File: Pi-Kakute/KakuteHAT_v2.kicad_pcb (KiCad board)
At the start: 2 copper layers, 65 x 56 mm, 49 parts, among them J1 40HAT, J12 FC_Socket, J2 ID_EEPROM, J3 I2C, J4 Mout1_2, J5 Mout3_4, J6 RC_IN, J7 GPS2, J8 Power_Pad, J9 FC_Socket2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

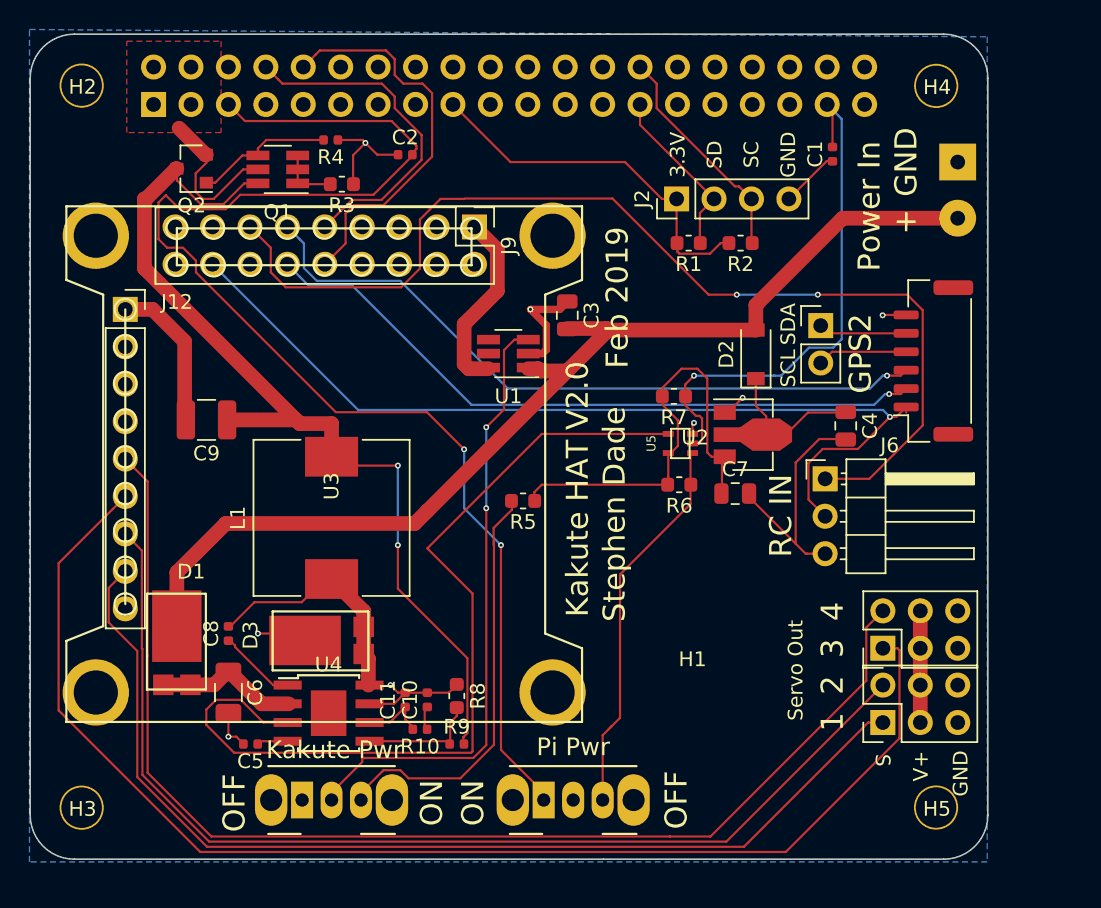
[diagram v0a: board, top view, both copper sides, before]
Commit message: Pi-Kakute: Added EEPROM and improved 40-pin header and mounting holes
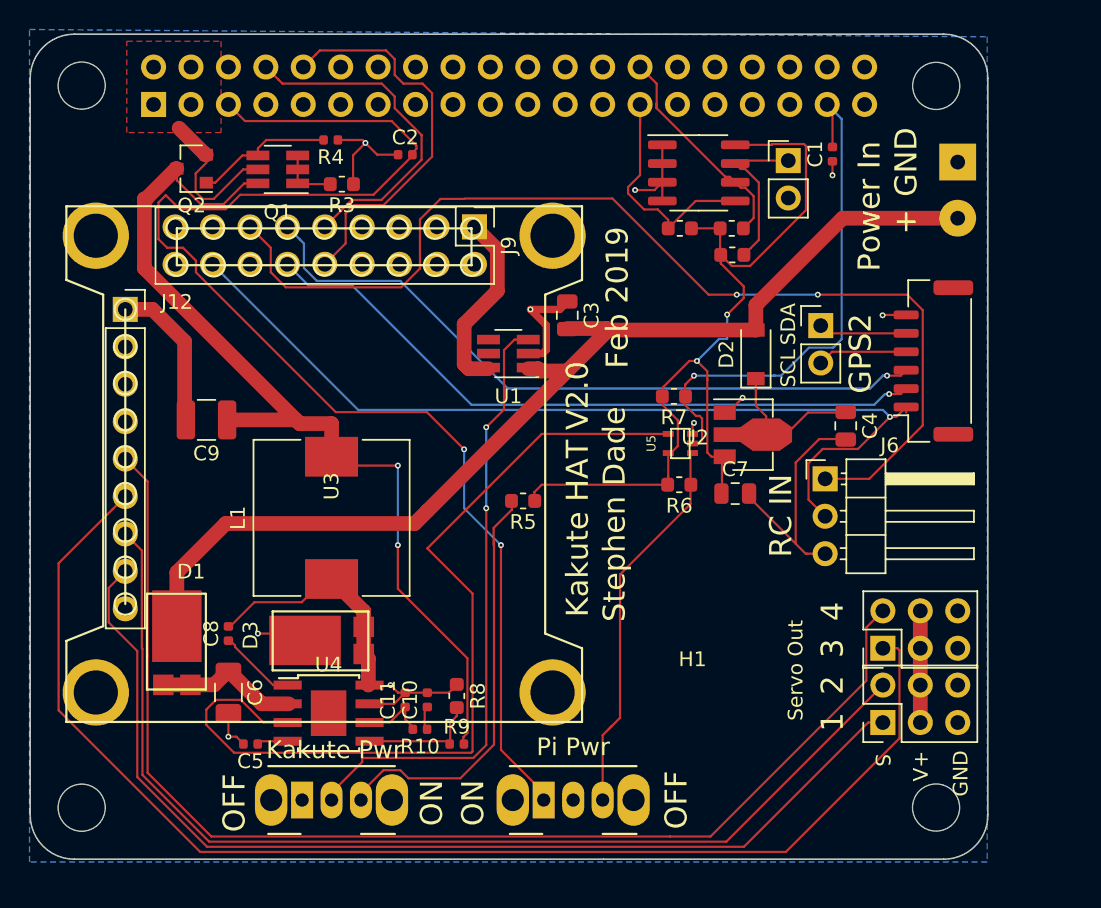
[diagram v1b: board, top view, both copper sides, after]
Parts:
- added R11: 10K, Resistor_SMD:R_0603_1608Metric, F.Cu at (126.2, 75.8)
- added U6: CAT24C32, Package_SO:SOIC-8_3.9x4.9mm_P1.27mm, F.Cu at (123.9, 70.2)
- H2, H3, H4, H5: footprint project_footprints:NPTH_3mm_ID -> MountingHole:MountingHole_3.2mm_M3_ISO7380
- J2: value ID_EEPROM -> Conn_01x02; footprint Connector_PinHeader_2.54mm:PinHeader_1x04_P2.54mm_Vertical -> Connector_PinHeader_2.54mm:PinHeader_1x02_P2.54mm_Vertical
- moved J2 8.01 mm to (130.0, 69.4), turned to 0 degrees
- moved R1 1.17 mm to (122.6, 74.0), turned to 0 degrees
- moved R2 1.17 mm to (126.2, 74.0)
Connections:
- J2 pad 1: /P3V3_HAT -> Net-(J2-Pad1)
- J2 pad 2: /ID_SD_EEPROM -> GND
- R1 pad 2: /P3V3_HAT -> VCC
- R2 pad 2: /P3V3_HAT -> VCC
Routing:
- net VCC: track 30.9 -> 61.8 mm, vias 0 -> 2
- net /P3V3_HAT: track 25.3 -> 0.00 mm
- net Net-(J2-Pad1): track 0.00 -> 11.1 mm
- net /ID_SD_EEPROM: track 11.9 -> 17.1 mm
- net GND: track 64.0 -> 66.8 mm, vias 8 -> 10
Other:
- board text removed: "3.3V"
- board text removed: "SC"
- board text removed: "SD"

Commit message: Pi-Kakute: Updated power input to match Pi-Connect
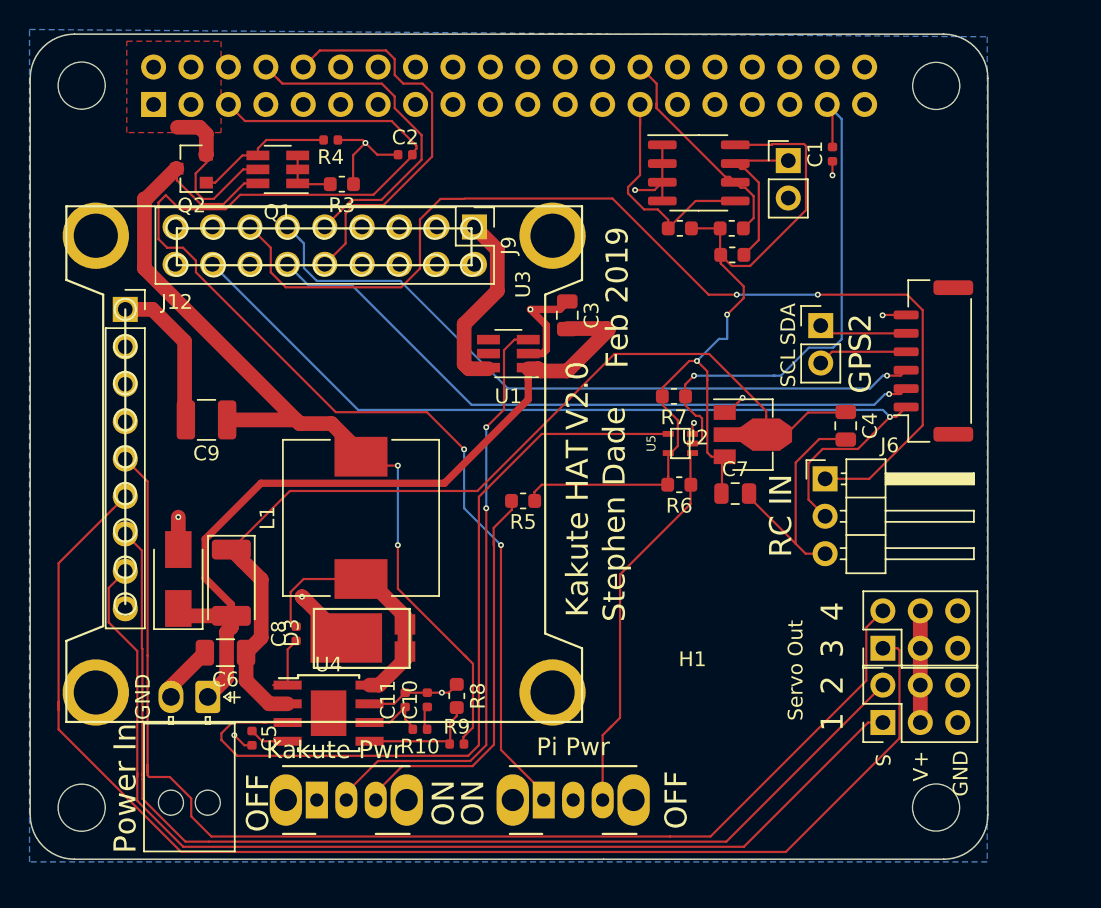
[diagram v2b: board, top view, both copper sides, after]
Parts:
- D1: value PDS560-13 -> 30V; footprint PowerDI:POWERDI5 -> Diode_SMD:D_SMA
- D2: value SMD-DIODE-100V-200MA_SOD-123_ -> D_Schottky; footprint Diode_SMD:D_SOD-123 -> Diode_SMD:D_2010_5025Metric
- J8: footprint Connector_Wire:SolderWirePad_1x02_P3.81mm_Drill1mm -> Connector_Molex:Molex_Nano-Fit_105313-xx02_1x02_P2.50mm_Horizontal
- SW1: value Pi Power Switch -> Kakute Power Switch
- moved J8 62.5 mm to (90.6, 105.8)
- moved D2 38.8 mm to (92.2, 98.0), turned to 270 degrees
- moved C8 4.60 mm to (96.6, 101.5)
- moved D1 3.50 mm to (88.6, 97.8), turned to 90 degrees
- moved D3 2.80 mm to (100.3, 101.8)
- moved C6 2.71 mm to (91.8, 102.8), turned to 180 degrees
- moved L1 2.00 mm to (101.0, 93.7)
- moved SW1 1.00 mm to (98.0, 112.8)
- moved C5 0.41 mm to (93.6, 108.6), turned to 270 degrees
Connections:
- C4 pad 1: Net-(C4-Pad1) -> /VIN_POST
- C6 pad 1: Net-(C6-Pad1) -> /VIN_POST
- D1 pad 1: Net-(C6-Pad1) -> /VIN_RAW
- D1 pad 2: /VIN_RAW -> GND
- D2 pad 1: Net-(C4-Pad1) -> /VIN_POST
- J8 pad 1: GND -> /VIN_RAW
- J8 pad 2: /VIN_RAW -> GND
- U2 pad 2: Net-(C4-Pad1) -> /VIN_POST
- U4 pad 2: Net-(C6-Pad1) -> /VIN_POST
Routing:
- net /VIN_POST: track 0.00 -> 67.3 mm
- net /VIN_RAW: track 73.1 -> 54.3 mm
- net Net-(C4-Pad1): track 12.8 -> 0.00 mm
- net Net-(C6-Pad1): track 10.3 -> 0.00 mm
- net /P_ENABLE: track 61.1 -> 55.2 mm
- net GND: track 66.8 -> 71.5 mm, vias 10 -> 11
- net Net-(R5-Pad2): track 28.6 -> 27.2 mm
- net /FC_M4: track 82.1 -> 83.4 mm
- net /FC_M3: track 87.8 -> 89.1 mm
- net /FC_M1: track 71.3 -> 72.5 mm
- net Net-(SW1-Pad2): track 41.7 -> 40.6 mm
- net Net-(C8-Pad1): track 5.42 -> 4.30 mm
- net /FC_M2: track 73.4 -> 74.4 mm
- net /P5V_HAT: track 10.7 -> 11.7 mm
- net Net-(C8-Pad2): track 17.0 -> 18.0 mm
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
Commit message: Pi-Kakute: Upgraded 3.3 Reg and Fixed RC/Mout pins
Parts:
- removed J5: Mout3_4, Connector_PinHeader_2.54mm:PinHeader_2x03_P2.54mm_Vertical
- added J10: Ext_Switch, Connector_PinHeader_2.54mm:PinHeader_1x03_P2.54mm_Vertical, F.Cu at (119.0, 101.6)
- added JP1: SolderJumper_3_Bridged12, Jumper:SolderJumper-3_P1.3mm_Bridged2Bar12_Pad1.0x1.5mm, F.Cu at (112.6, 99.8)
- J4: value Mout1_2 -> Mout; footprint Connector_PinHeader_2.54mm:PinHeader_2x03_P2.54mm_Vertical -> Kakute:PinHeader_4x03_P2.54mm_Horizontal
- U2: value AP2204RA-3.3 -> TPS709; footprint Package_TO_SOT_SMD:SOT-89-3 -> Package_TO_SOT_SMD:SOT-23-5_HandSoldering
- moved J4 10.3 mm to (133.9, 97.5), turned to 0 degrees
- moved C7 9.34 mm to (128.0, 82.8), turned to 90 degrees
- moved J6 7.34 mm to (139.0, 87.6)
- moved J7 5.20 mm to (140.0, 77.8)
- moved C4 2.15 mm to (131.8, 86.9)
- moved U2 1.18 mm to (127.8, 87.0)
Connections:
- J1 pad 1: /P3V3_HAT -> (no net)
- J1 pad 17: /P3V3_HAT -> (no net)
- J4 pad 1: /FC_M1 -> /FC_M4
- J4 pad 2: /FC_M2 -> /MOUT_V
- J4 pad 3: /MOUT_V -> GND
- J4 pad 4: /MOUT_V -> /FC_M3
- J4 pad 5: GND -> /MOUT_V
- R6 pad 1: Net-(R6-Pad1) -> VCC
- R6 pad 2: VCC -> Net-(J10-Pad1)
- SW2 pad 1: /PI_OFF -> Net-(J10-Pad1)
- SW2 pad 2: GND -> Net-(JP1-Pad1)
- SW2 pad 3: Net-(R6-Pad1) -> /PI_OFF
- U2 pad 1: GND -> /VIN_POST
- U2 pad 2: /VIN_POST -> GND
- U2 pad 3: VCC -> (no net)
- U5 pad 1: Net-(R6-Pad1) -> Net-(J10-Pad1)
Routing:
- net Net-(J10-Pad1): track 0.00 -> 36.9 mm
- net Net-(R6-Pad1): track 26.3 -> 0.00 mm
- net Net-(JP1-Pad1): track 0.00 -> 13.8 mm
- net GND: track 71.5 -> 59.3 mm, vias 11 -> 14
- net Net-(J10-Pad2): track 0.00 -> 10.0 mm
- net /RC_IN: track 72.0 -> 64.2 mm
- net VCC: track 61.8 -> 67.8 mm
- net /FC_GPS_TX: track 46.4 -> 51.7 mm
- net /FC_GPS_RX: track 48.0 -> 53.3 mm
- net /VIN_POST: track 67.3 -> 62.9 mm, vias 0 -> 2
- net /PI_OFF: track 89.7 -> 86.1 mm
- net Net-(J3-Pad2): track 6.12 -> 8.78 mm
- net Net-(J3-Pad1): track 6.17 -> 8.63 mm
- net /FC_M4: track 83.4 -> 85.4 mm
- net /FC_5V: track 62.5 -> 64.3 mm
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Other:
- board text added: "+V"
- board text added: "5V"
- board text removed: "V+"

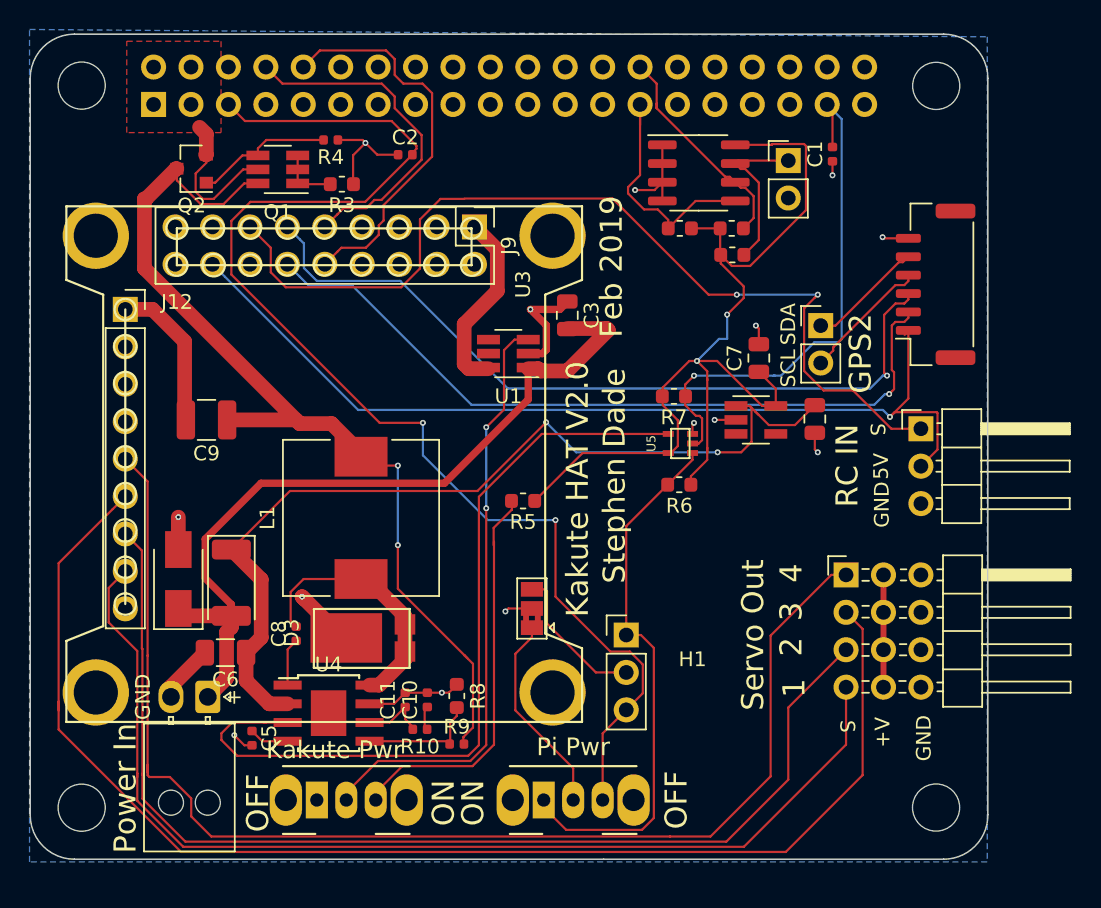
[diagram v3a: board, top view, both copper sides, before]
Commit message: Pi-Kakute: Label Cleanup
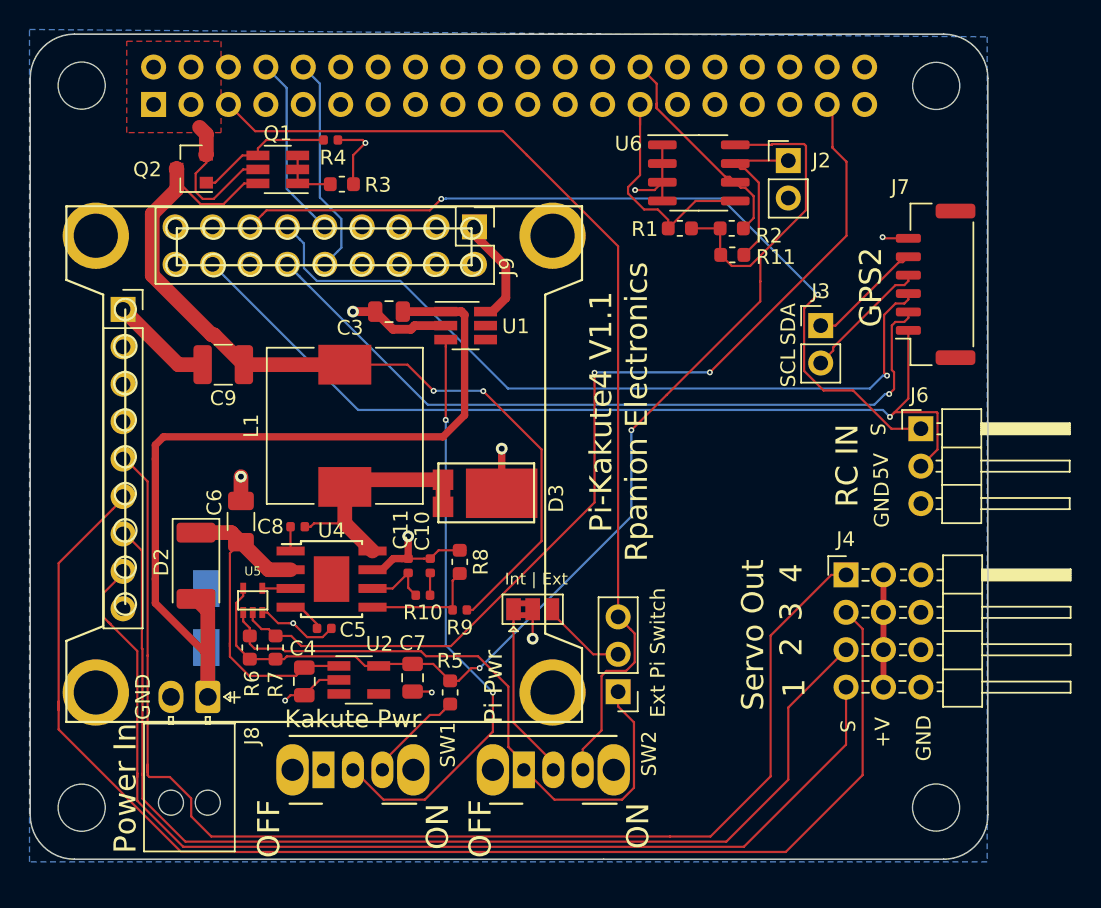
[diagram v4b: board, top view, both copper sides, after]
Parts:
- removed C1, C2: 0.1uF, Capacitor_SMD:C_0402_1005Metric
- C6: value 10uF, 1mOhm, 50V, 5A IRMS, X7R -> 10uF, 50V
- D1: moved to B.Cu
- J2: value Conn_01x02 -> EEPROM_W
- moved C4 39.0 mm to (97.2, 104.8)
- moved U2 32.2 mm to (100.8, 104.7)
- moved C7 32.0 mm to (104.5, 104.5), turned to 270 degrees
- moved R7 32.0 mm to (95.2, 102.5), turned to 270 degrees
- moved R6 31.2 mm to (93.5, 102.5), turned to 90 degrees
- moved U5 30.9 mm to (93.7, 99.2), turned to 0 degrees
- moved D3 14.0 mm to (110.2, 92.0), turned to 270 degrees
- moved R5 13.9 mm to (107.0, 105.5), turned to 270 degrees
- moved C3 12.1 mm to (102.9, 79.7), turned to 0 degrees
- moved C10 9.10 mm to (105.7, 96.9)
- moved C11 9.10 mm to (104.2, 96.9)
- moved R10 9.10 mm to (105.2, 98.9)
- moved R8 9.10 mm to (107.7, 96.6)
- moved R9 9.10 mm to (107.7, 99.9)
- moved U4 9.10 mm to (99.0, 97.8)
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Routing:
- net /P_ENABLE: track 55.2 -> 1.93 mm
- net /VIN_POST: track 62.9 -> 24.0 mm, vias 2 -> 0
- net /PWR_OFF: track 36.5 -> 67.7 mm, vias 1 -> 2
- net Net-(R5-Pad2): track 27.2 -> 6.74 mm
- net /PI_OFF: track 86.1 -> 68.9 mm, vias 2 -> 0
- net /TELE_TO_PI: track 26.7 -> 14.9 mm
- net VCC: track 67.8 -> 79.0 mm
- net /TELE_TO_FC: track 23.1 -> 12.5 mm
- net /RC_IN: track 64.2 -> 57.8 mm
- net GND: track 59.3 -> 52.9 mm, vias 14 -> 11
- net Net-(J10-Pad1): track 36.9 -> 42.8 mm
- net /VIN_RAW: track 54.3 -> 59.9 mm
- net Net-(J9-Pad1): track 12.7 -> 7.47 mm
- net /P5V: track 64.7 -> 60.4 mm
- net Net-(J10-Pad2): track 10.0 -> 5.91 mm
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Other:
- board text added: "Ext Pi Switch"
- board text added: "Int | Ext"
- board text added: "Pi-Kakute4 V1.1 Rpanion Electronics"
- board text removed: "Feb 2019"
- board text removed: "Kakute HAT V2.0"
- board text removed: "Stephen Dade"
